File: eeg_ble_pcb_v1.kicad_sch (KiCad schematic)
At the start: 3 parts, among them U1 STM32WB55RGVx

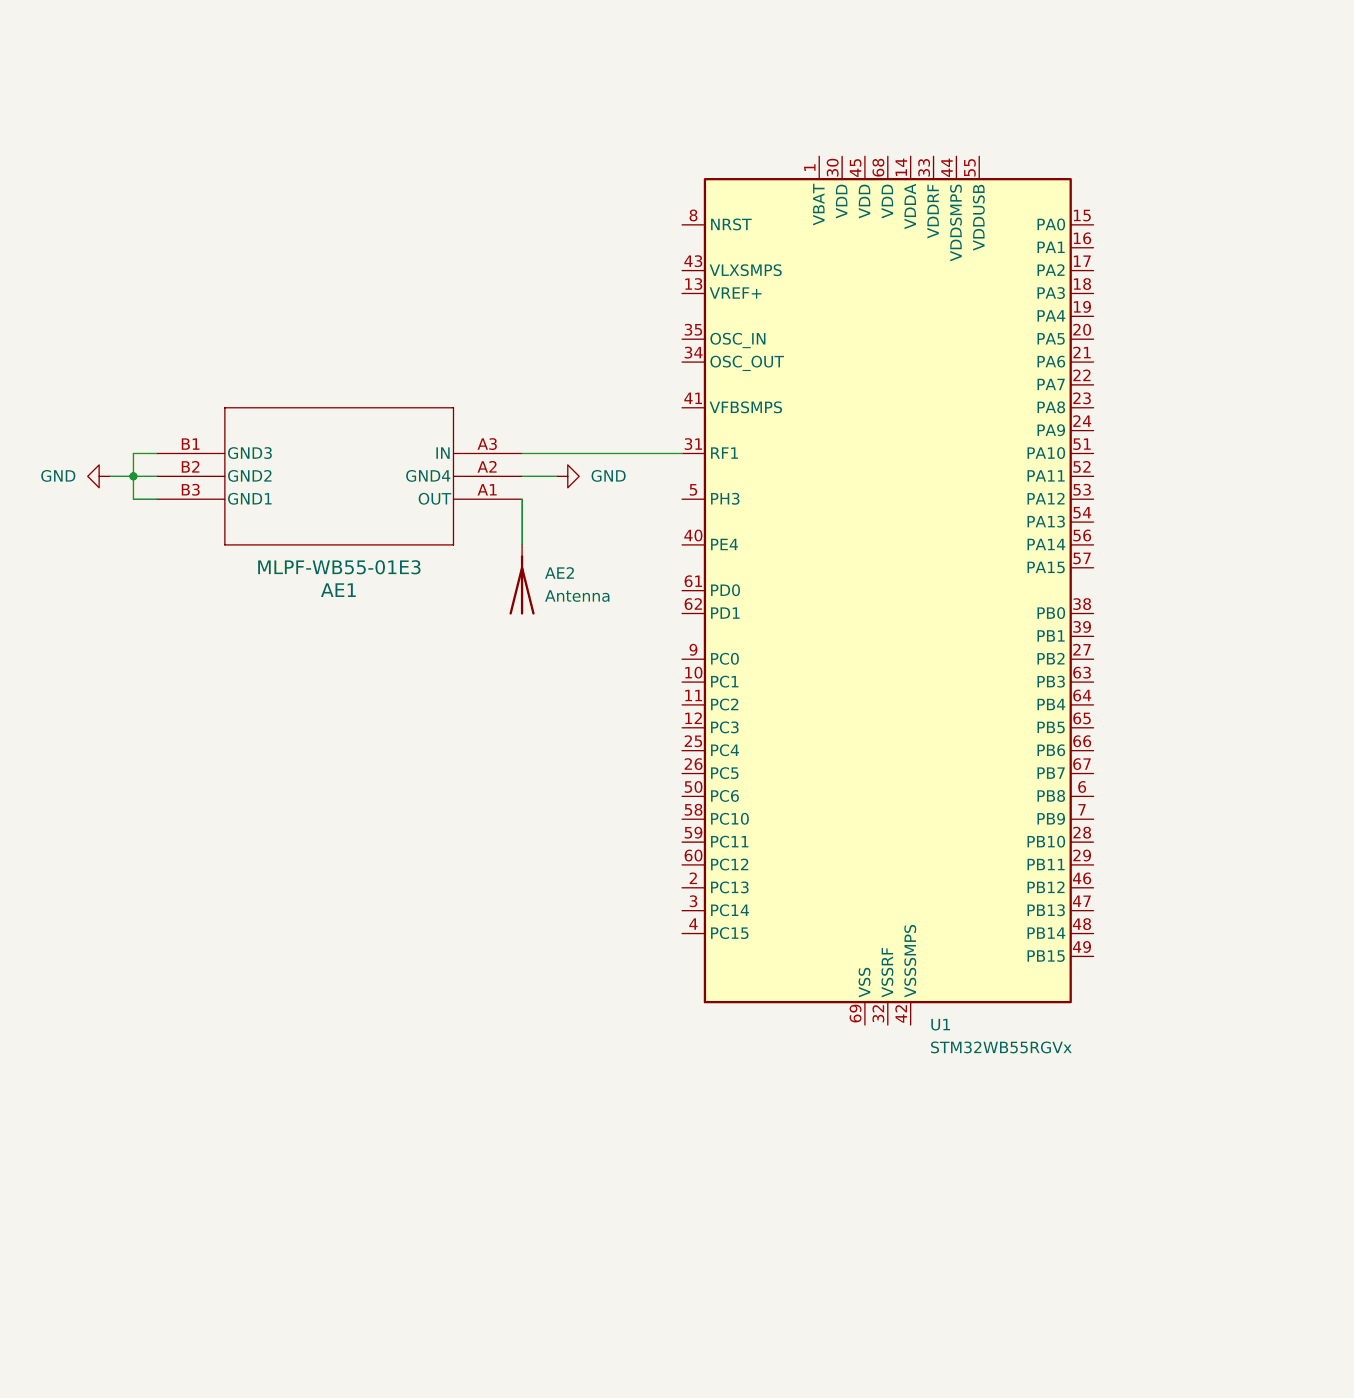
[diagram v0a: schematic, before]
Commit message: Decoupling capacitors and NRST
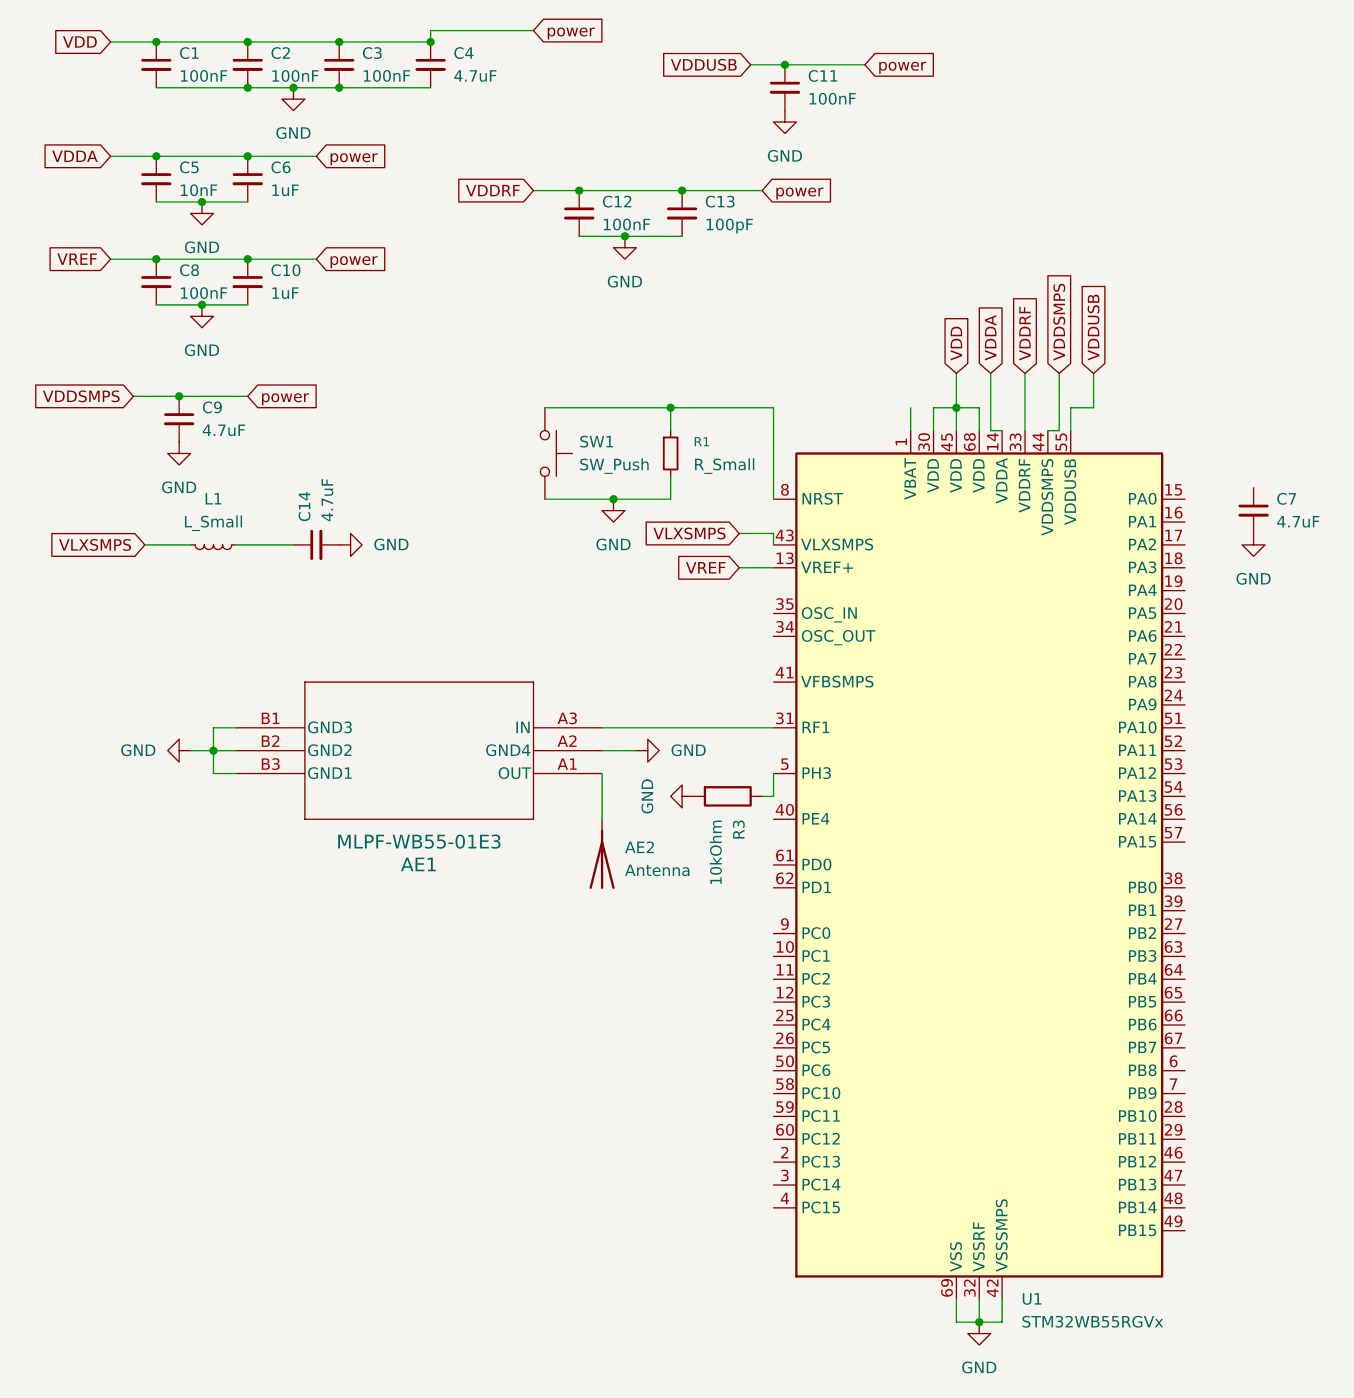
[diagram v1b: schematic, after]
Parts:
- added C1, C11, C12, C2, C3, C8: 100nF, symbol Device:C_Small
- added C10, C6: 1uF, symbol Device:C_Small
- added C13: 100pF, symbol Device:C_Small
- added C14, C4, C7, C9: 4.7uF, symbol Device:C_Small
- added C5: 10nF, symbol Device:C_Small
- added L1: L_Small, symbol Device:L_Small
- added R1: R_Small, symbol Device:R_Small
- added R3: 10kOhm, Resistor_SMD:R_0805_2012Metric_Pad1.20x1.40mm_HandSolder, symbol Device:R
- added SW1: SW_Push, symbol Switch:SW_Push
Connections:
- net GND: now also U1.32 (VSSRF), U1.42 (VSSSMPS), U1.69 (VSS), C1.2, C10.2, C11.2, C12.2, C13.2, C14.2, C2.2, C3.2, C4.2, C5.2, C6.2, C7.2, C8.2, C9.2, R1.2, R3.2, SW1.2
- net VDD: now reaches U1.13 (VREF+)
- net VDD: now also U1.14 (VDDA), U1.30 (VDD), U1.33 (VDDRF), U1.44 (VDDSMPS), U1.45 (VDD), U1.55 (VDDUSB), U1.68 (VDD), C1.1, C10.1, C11.1, C12.1, C13.1, C2.1, C3.1, C4.1, C5.1, C6.1, C8.1, C9.1
- net VLXSMPS: now reaches U1.43 (VLXSMPS)
- net VLXSMPS: now also L1.2
- net at U1.5 (PH3): now also R3.1
- net at U1.8 (NRST): now also R1.1, SW1.1
- new net: C14.1, L1.1
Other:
- moved on the sheet: AE1, AE2, U1

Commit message: Added oscillator
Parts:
- removed C14, C7: 4.7uF, symbol Device:C_Small
- removed L1: L_Small, symbol Device:L_Small
- added X1: NX2016SA-32MHZ-EXS00A-CS06654, NX2016SA_NDK, symbol 395_project_library:NX2016SA-32MHZ-EXS00A-CS06654
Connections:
- net GND: now also X1.2, X1.4
- net VDD: now also U1.1 (VBAT)
- net at U1.34 (OSC_OUT): now also X1.3
- net at U1.35 (OSC_IN): now also X1.1
- net VLXSMPS: no longer names the net of U1.43 (VLXSMPS)
- no-connect marks 0 -> 2
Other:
- moved on the sheet: AE1, AE2, R3

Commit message: Addded BMS
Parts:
- added C14: 0.1u, symbol Device:C
- added C15, C7: 10u, symbol Device:C
- added C16: 1n, symbol Device:C
- added D1: LED_green, symbol Device:LED
- added D2: LED_red, symbol Device:LED
- added J1: USB_C_Receptacle_USB2.0_16P, symbol Connector:USB_C_Receptacle_USB2.0_16P
- added Q1: FS8205, FS8205:SOT95P280X145-6N, symbol My_lib:FS8205
- added R2 (x2), R4: 1k, symbol Device:R
- added R4: 1.2k, symbol Device:R
- added R5: 100, symbol Device:R
- added R6, R7: 5.1k, symbol Device:R
- added R8: 1M, symbol Device:R
- added U2: TP4056-42-ESOP8, Package_SO:SOIC-8-1EP_3.9x4.9mm_P1.27mm_EP2.41x3.3mm_ThermalVias, symbol Battery_Management:TP4056-42-ESOP8
- added U2: DW01A, Package_TO_SOT_SMD:SOT-23-6, symbol Battery_Management:DW01A
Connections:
- net GND: now also C15.2, C16.1, C7.2, J1.A1 (GND), J1.A12 (GND), J1.B1 (GND), J1.B12 (GND), Q1.3, R4.1, R4.2, R6.2, R7.2, R8.1, U2.1 (TEMP), U2.3 (GND)
- new net: D1.1 (K), R2.1
- new net: R2.2, U2.6 (~{STDBY})
- new net: R4.2, U2.2 (PROG)
- new net: C14.1, R5.2, U2.5 (VCC)
- new net: J1.A5 (CC1), R7.1
- new net: R4.1, U2.2 (CS)
- new net: R2.1, U2.7 (~{CHRG})
- new net: Q1.2, Q1.5
- new net: Q1.4, U2.3 (OC)
- new net: Q1.6, U2.1 (OD)
- new net: D2.1 (K), R2.2
- new net: J1.B5 (CC2), R6.1
- new net +5V: C7.1, D1.2 (A), D2.2 (A), J1.A4 (VBUS), J1.A9 (VBUS), J1.B4 (VBUS), J1.B9 (VBUS), U2.4 (V_{CC}), U2.8 (CE)
- new net B+: C15.1, R5.1, U2.5 (BAT)
- new net B-: C14.2, Q1.1, U2.6 (GND)
- new net Chasis: C16.2, J1.S1 (SHIELD), R8.2
- no-connect marks 2 -> 8
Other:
- moved on the sheet: AE1, AE2, C1, C10, C11, C12, C13, C2, C3, C4, C5, C6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

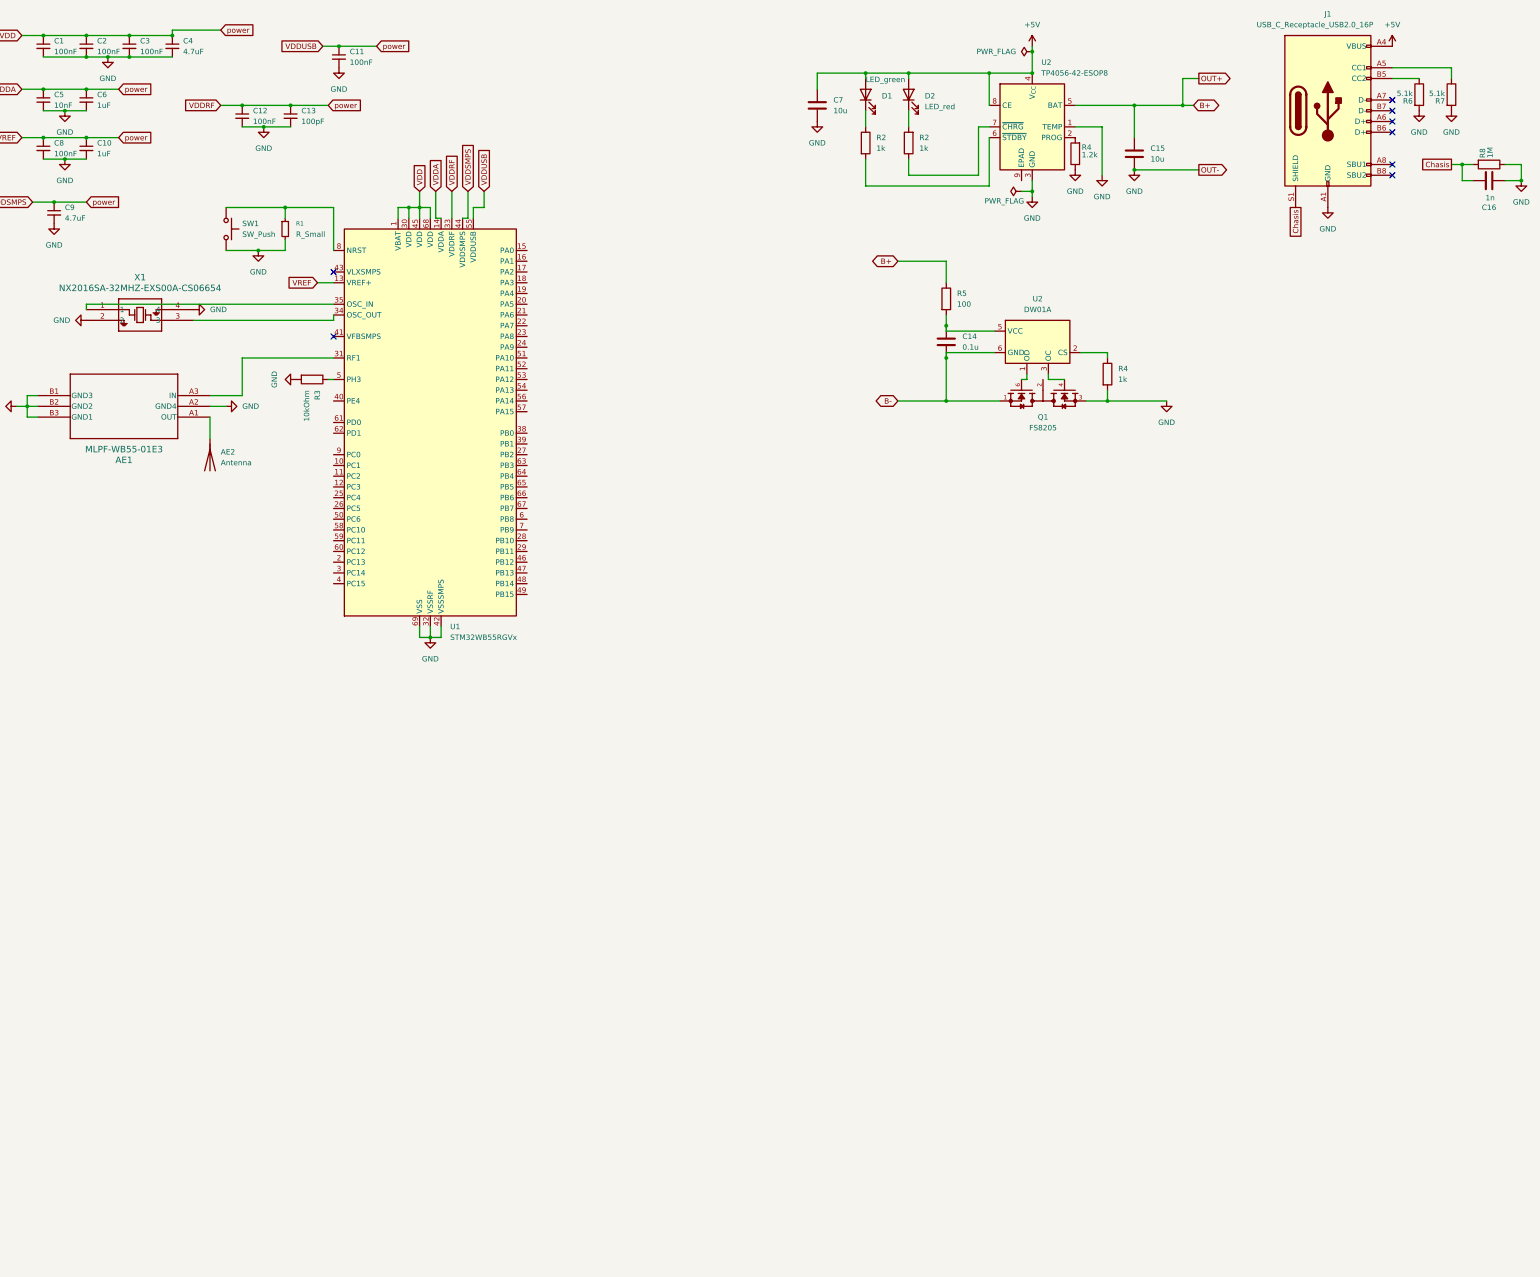
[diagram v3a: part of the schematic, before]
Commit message: BMS and footprint sync
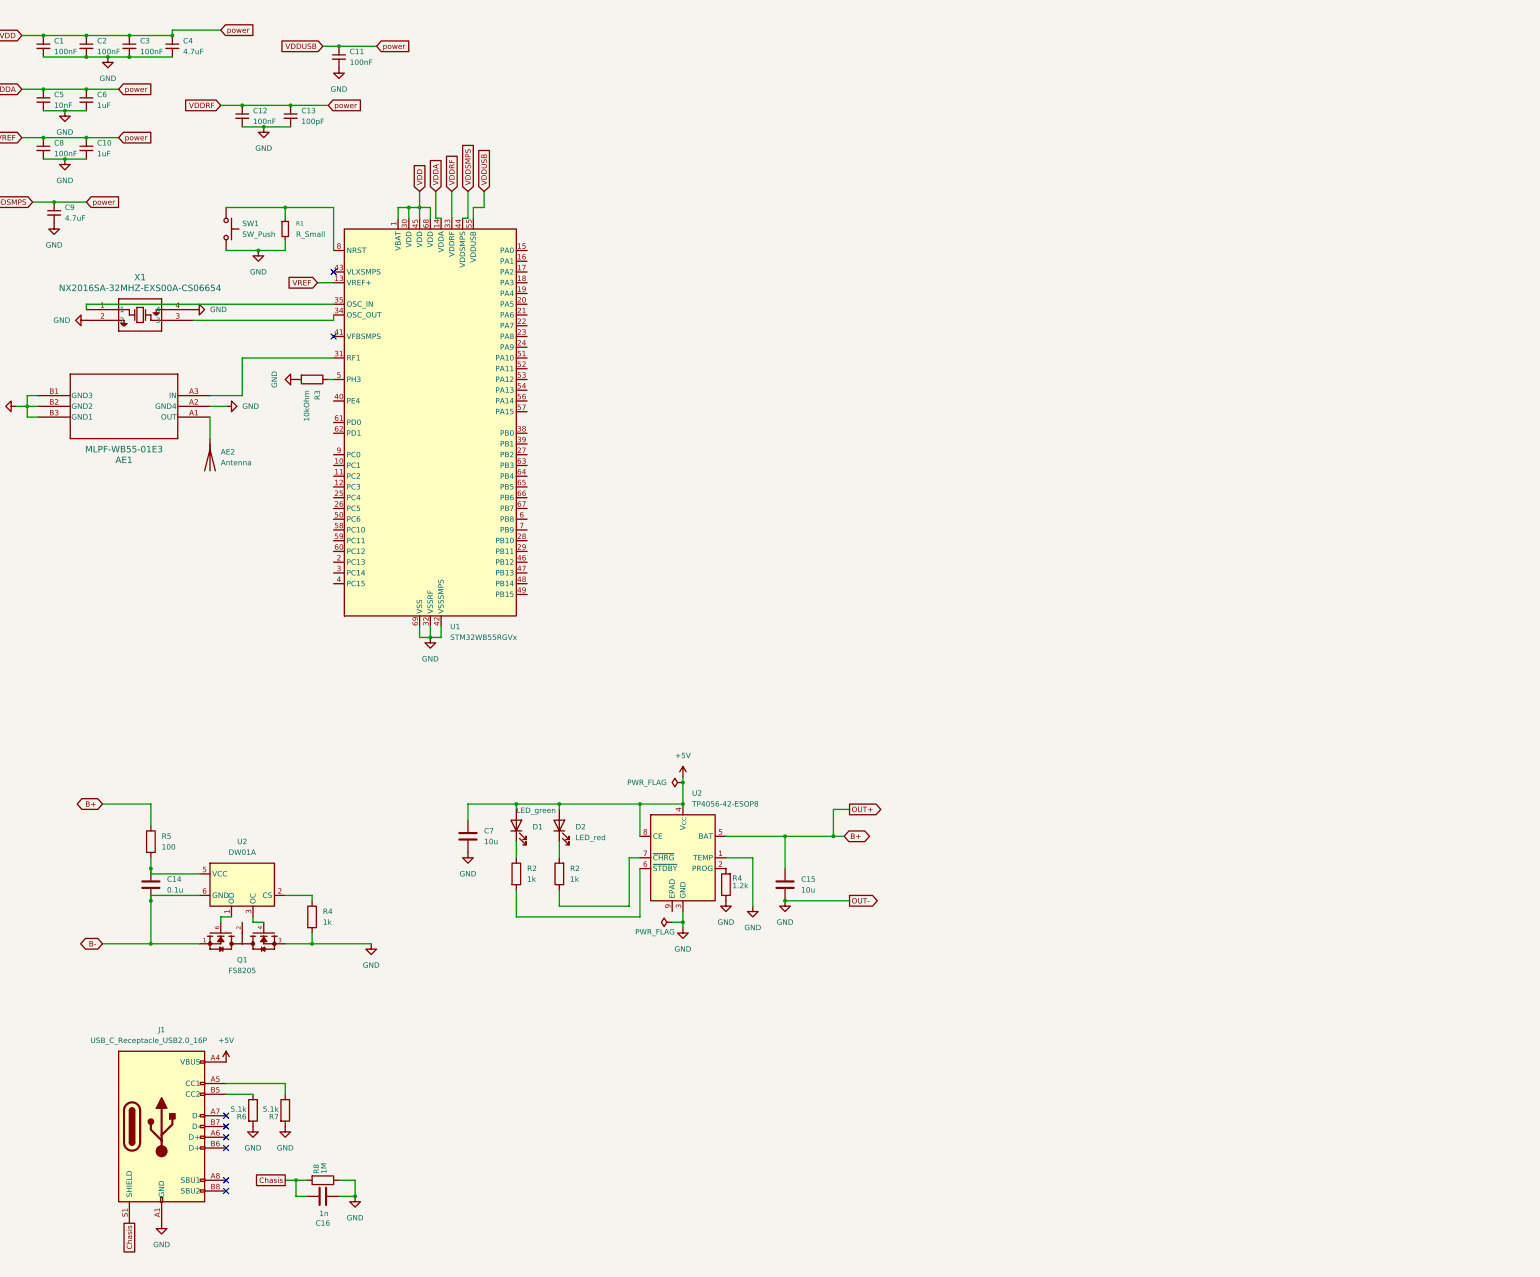
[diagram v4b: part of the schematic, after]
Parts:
- removed Q1: FS8205, FS8205:SOT95P280X145-6N, symbol My_lib:FS8205
- added Q1: FS8205, FS8205:SOT95P280X145-6N, symbol 395_project_library:FS8205
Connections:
- net B-: now also Q1.1
- net GND: now also Q1.3
- net at U2.3 (OC): now also Q1.4
- net at U2.1 (OD): now also Q1.6
- new net: Q1.2, Q1.5
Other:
- moved on the sheet: C14, C15, C16, C7, D1, D2, J1, R2, R4, R5, R6, R7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
